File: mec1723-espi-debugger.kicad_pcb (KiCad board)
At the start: 8 copper layers, 62 x 87 mm, 239 parts, among them J1 PinHeader_2x6_P2.54mm_Drill1.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, J10 PinHeader_2x5_P1.27mm_SMD, J11 PinHeader_2x5_P1.27mm_SMD, J12 PinHeader_2x5_P1.27mm_SMD, J13 Tag-Connect_TC2050-IDC-NL_2x5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, J14 Tag-Connect_TC2050-IDC-NL_2x5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, J15 USB-C_GCT_USB4105-GF-A, J2 PinHeader_2x5_P1.27mm_SMD, J3 PinHeader_2x5_P1.27mm_SMD, J4 PinHeader_2x5_P1.27mm_SMD, J5 PinHeader_2x5_P1.27mm_SMD, J6 PinHeader_2x5_P1.27mm_SMD, J7 PinHeader_2x5_P1.27mm_SMD, J8 PinHeader_2x5_P1.27mm_SMD, J9 PinHeader_2x5_P1.27mm_SMD, Q1 DMG1012T-7, SW1 SW_KSC441J70SHLFS_SMD, SW2 SW_KSC441J70SHLFS_SMD, SW3 SW_KSC441J70SHLFS_SMD, U1 MEC1723N-B0-I/SZ, U2 TLV76701_WSON, U3 TPS566231P, U4 MT25QU01GBBB8_SOIC, U5 SN74AC7541_VQFN, U6 SN74AC7541_VQFN, U7 FT2232HL-REEL, Y1 Resonator_32.768kHz_ECX-31B, Y2 Resonator_12MHz_KX-7

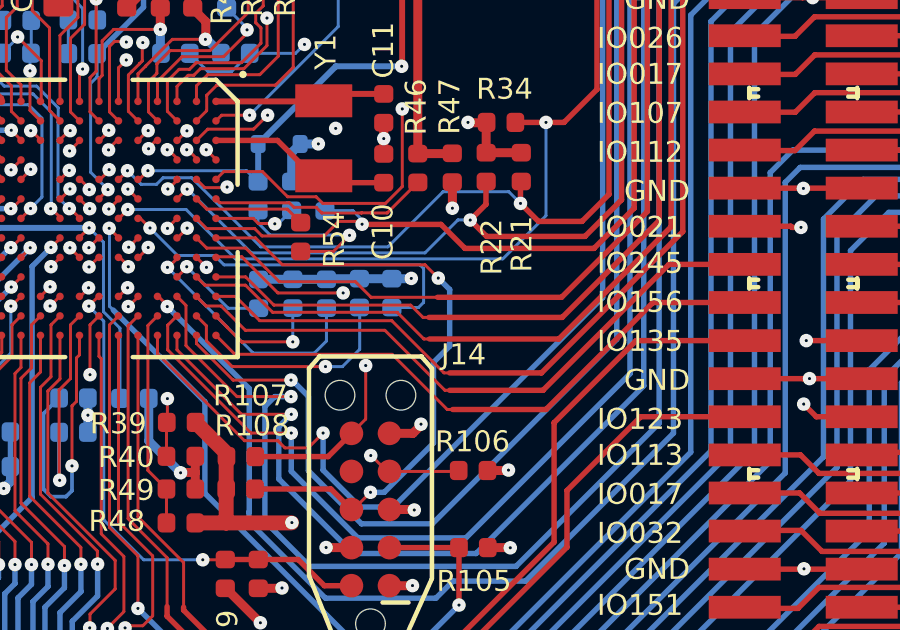
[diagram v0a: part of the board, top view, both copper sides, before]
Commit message: [#103697] pcb: move GPIO156 trace further from the tag-connect hole
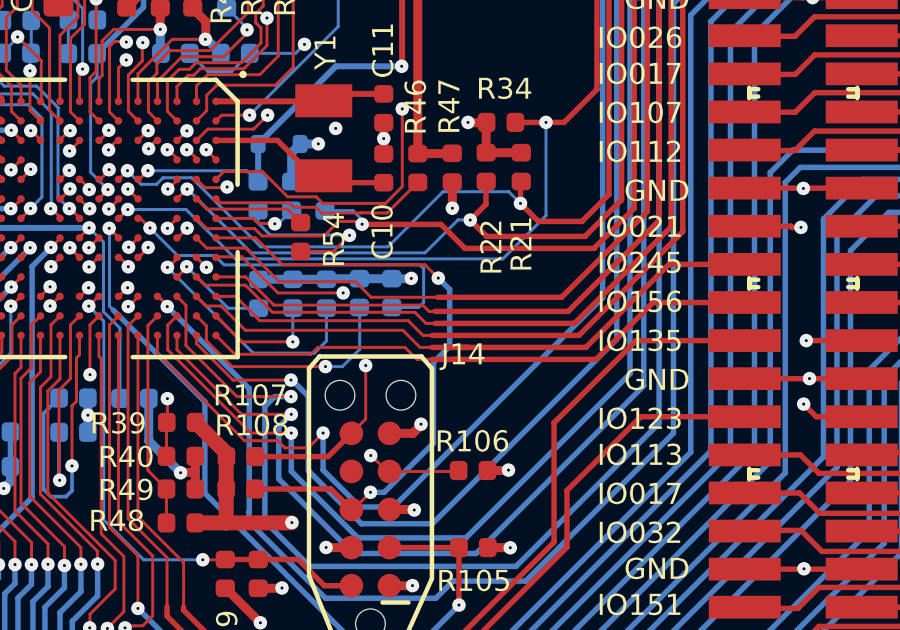
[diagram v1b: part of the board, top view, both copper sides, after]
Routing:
- net /MEC1723/GPIO224: track 44.7 -> 43.6 mm
- net /MEC1723/GPIO156: track 20.1 -> 19.1 mm
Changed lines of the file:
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@@
 	)
 	(segment
-		(start 95.305467 110.656213)
-		(end 98.87168 107.09)
+		(start 98.87168 107.09)
+		(end 101.931 107.09)
+		(width 0.182)
+		(layer "F.Cu")
+		(net "/MEC1723/GPIO156")
+	)
+	(segment
+		(start 92.405467 108.986213)
+		(end 91.505467 108.986213)
 		(width 0.182)
 		(layer "F.Cu")
@@
 	)
 	(segment
-		(start 92.195467 110.656213)
-		(end 92.015467 110.656213)
+		(start 84.305467 108.186213)
+		(end 84.935467 108.816213)
 		(width 0.1)
 		(layer "F.Cu")
@@
 	)
 	(segment
-		(start 92.195467 110.656213)
-		(end 95.305467 110.656213)
+		(start 92.205467 108.986213)
+		(end 92.405467 108.986213)
 		(width 0.182)
 		(layer "F.Cu")
@@
 	)
 	(segment
-		(start 90.175467 108.816213)
-		(end 84.935467 108.816213)
+		(start 90.605467 108.586213)
+		(end 91.005467 108.986213)
 		(width 0.1)
 		(layer "F.Cu")
@@
 	)
 	(segment
-		(start 84.935467 108.816213)
-		(end 84.305467 108.186213)
+		(start 87.475467 108.816213)
+		(end 87.705467 108.586213)
 		(width 0.1)
 		(layer "F.Cu")
@@
 	)
 	(segment
-		(start 98.87168 107.09)
-		(end 101.931 107.09)
+		(start 96.975467 108.986213)
+		(end 98.87168 107.09)
+		(width 0.182)
+		(layer "F.Cu")
+		(net "/MEC1723/GPIO156")
+	)
+	(segment
+		(start 92.405467 108.986213)
+		(end 96.975467 108.986213)
 		(width 0.182)
 		(layer "F.Cu")
@@
 	)
 	(segment
-		(start 92.015467 110.656213)
-		(end 90.175467 108.816213)
+		(start 84.935467 108.816213)
+		(end 87.475467 108.816213)
+		(width 0.1)
+		(layer "F.Cu")
+		(net "/MEC1723/GPIO156")
+	)
+	(segment
+		(start 87.705467 108.586213)
+		(end 90.605467 108.586213)
+		(width 0.1)
+		(layer "F.Cu")
+		(net "/MEC1723/GPIO156")
+	)
+	(segment
+		(start 91.005467 108.986213)
+		(end 91.505467 108.986213)
 		(width 0.1)
 		(layer "F.Cu")
@@
 	)
 	(segment
-		(start 99.772389 76.609291)
-		(end 99.075467 77.306213)
-		(width 0.182)
+		(start 85.295467 106.236213)
+		(end 86.235467 107.176213)
+		(width 0.1)
 		(layer "F.Cu")
 		(net "/MEC1723/GPIO242")
 	)
 	(segment
-		(start 84.305467 106.236213)
-		(end 85.295467 106.236213)
+		(start 91.405467 107.386213)
+		(end 91.605467 107.386213)
 		(width 0.1)
 		(layer "F.Cu")
@@
 	)
 	(segment
-		(start 95.845467 107.586213)
-		(end 91.405467 107.586213)
-		(width 0.182)
+		(start 91.195467 107.176213)
+		(end 91.405467 107.386213)
+		(width 0.1)
 		(layer "F.Cu")
 		(net "/MEC1723/GPIO242")
@@
 	)
 	(segment
-		(start 85.295467 106.236213)
-		(end 86.235467 107.176213)
-		(width 0.1)
-		(layer "F.Cu")
-		(net "/MEC1723/GPIO242")
-	)
-	(segment
-		(start 90.795467 107.176213)
-		(end 91.205467 107.586213)
-		(width 0.1)
-		(layer "F.Cu")
-		(net "/MEC1723/GPIO242")
-	)
-	(segment
 		(start 99.075467 77.306213)
 		(end 99.075467 104.356213)
@@
 	(segment
 		(start 99.075467 104.356213)
-		(end 95.845467 107.586213)
+		(end 96.045467 107.386213)
 		(width 0.182)
 		(layer "F.Cu")
@@
 	(segment
 		(start 86.235467 107.176213)
-		(end 90.795467 107.176213)
+		(end 91.195467 107.176213)
 		(width 0.1)
 		(layer "F.Cu")
@@
 	)
 	(segment
-		(start 91.205467 107.586213)
-		(end 91.405467 107.586213)
-		(width 0.1)
+		(start 96.045467 107.386213)
+		(end 91.605467 107.386213)
+		(width 0.182)
 		(layer "F.Cu")
 		(net "/MEC1723/GPIO242")
 	)
 	(segment
-		(start 99.865467 80.916213)
-		(end 99.865467 104.726213)
+		(start 99.772389 76.609291)
+		(end 99.075467 77.306213)
 		(width 0.182)
 		(layer "F.Cu")
-		(net "/MEC1723/GPIO224")
+		(net "/MEC1723/GPIO242")
 	)
 	(segment
-		(start 84.305467 106.886213)
-		(end 84.955467 106.886213)
+		(start 84.305467 106.236213)
+		(end 85.295467 106.236213)
 		(width 0.1)
 		(layer "F.Cu")
-		(net "/MEC1723/GPIO224")
+		(net "/MEC1723/GPIO242")
 	)
 	(segment
-		(start 85.765467 107.696213)
-		(end 90.165467 107.696213)
+		(start 84.955467 106.886213)
+		(end 85.765467 107.696213)
 		(width 0.1)
 		(layer "F.Cu")
@@
 	)
 	(segment
-		(start 84.955467 106.886213)
-		(end 85.765467 107.696213)
-		(width 0.1)
+		(start 91.505467 108.186213)
+		(end 96.405467 108.186213)
+		(width 0.182)
 		(layer "F.Cu")
 		(net "/MEC1723/GPIO224")
 	)
 	(segment
-		(start 91.905467 109.436213)
-		(end 92.095467 109.436213)
+		(start 91.205467 108.186213)
+		(end 91.505467 108.186213)
 		(width 0.1)
 		(layer "F.Cu")
@@
 	)
 	(segment
-		(start 90.165467 107.696213)
-		(end 91.905467 109.436213)
+		(start 99.865467 80.916213)
+		(end 99.865467 104.726213)
+		(width 0.182)
+		(layer "F.Cu")
+		(net "/MEC1723/GPIO224")
+	)
+	(segment
+		(start 90.715467 107.696213)
+		(end 91.205467 108.186213)
 		(width 0.1)
 		(layer "F.Cu")
@@
 	(segment
 		(start 99.865467 104.726213)
-		(end 95.155467 109.436213)
+		(end 96.405467 108.186213)
 		(width 0.182)
 		(layer "F.Cu")
@@
 	)
 	(segment
-		(start 95.155467 109.436213)
-		(end 92.095467 109.436213)
-		(width 0.182)
+		(start 84.305467 106.886213)
+		(end 84.955467 106.886213)
+		(width 0.1)
 		(layer "F.Cu")
 		(net "/MEC1723/GPIO224")
@@
 	)
 	(segment
+		(start 85.765467 107.696213)
+		(end 90.715467 107.696213)
+		(width 0.1)
+		(layer "F.Cu")
+		(net "/MEC1723/GPIO224")
+	)
+	(segment
 		(start 85.765467 99.496213)
 		(end 86.38 98.88168)
@@
 	)
 	(segment
-		(start 86.192625 107.416213)
+		(start 96.255467 107.786213)
+		(end 91.945467 107.786213)
+		(width 0.182)
+		(layer "F.Cu")
+		(net "/MEC1723/GPIO246")
+	)
+	(segment
+		(start 90.305467 107.416213)
 		(end 90.345467 107.416213)
 		(width 0.1)
@@
 	)
 	(segment
-		(start 99.475467 79.746213)
-		(end 99.475467 104.566213)
+		(start 91.945467 107.786213)
+		(end 91.605467 107.786213)
 		(width 0.182)
 		(layer "F.Cu")
@@
 	)
 	(segment
-		(start 90.345467 107.416213)
-		(end 91.235467 108.306213)
+		(start 86.192625 107.416213)
+		(end 90.305467 107.416213)
 		(width 0.1)
 		(layer "F.Cu")
@@
 	)
 	(segment
-		(start 91.385467 108.306213)
-		(end 91.405467 108.286213)
-		(width 0.1)
+		(start 100.074389 79.147291)
+		(end 99.475467 79.746213)
+		(width 0.182)
 		(layer "F.Cu")
 		(net "/MEC1723/GPIO246")
@@
 	)
 	(segment
-		(start 85.287625 106.511213)
-		(end 86.192625 107.416213)
+		(start 99.475467 79.746213)
+		(end 99.475467 104.566213)
+		(width 0.182)
+		(layer "F.Cu")
+		(net "/MEC1723/GPIO246")
+	)
+	(segment
+		(start 90.935467 107.416213)
+		(end 91.305467 107.786213)
 		(width 0.1)
 		(layer "F.Cu")
@@
 	)
 	(segment
-		(start 101.933314 79.147291)
-		(end 100.074389 79.147291)
+		(start 99.475467 104.566213)
+		(end 96.255467 107.786213)
 		(width 0.182)
 		(layer "F.Cu")
@@
 	)
 	(segment
+		(start 85.287625 106.511213)
+		(end 86.192625 107.416213)
+		(width 0.1)
+		(layer "F.Cu")
+		(net "/MEC1723/GPIO246")
+	)
+	(segment
 		(start 83.930467 106.511213)
 		(end 85.287625 106.511213)
@@
 	)
 	(segment
-		(start 91.235467 108.306213)
-		(end 91.385467 108.306213)
+		(start 91.305467 107.786213)
+		(end 91.945467 107.786213)
 		(width 0.1)
 		(layer "F.Cu")
@@
 	)
 	(segment
-		(start 95.735467 108.306213)
-		(end 91.425467 108.306213)
-		(width 0.182)
+		(start 90.305467 107.416213)
+		(end 90.935467 107.416213)
+		(width 0.1)
 		(layer "F.Cu")
 		(net "/MEC1723/GPIO246")
 	)
 	(segment
-		(start 99.475467 104.566213)
-		(end 95.735467 108.306213)
+		(start 101.933314 79.147291)
+		(end 100.074389 79.147291)
 		(width 0.182)
 		(layer "F.Cu")
@@
 	)
 	(segment
-		(start 100.074389 79.147291)
-		(end 99.475467 79.746213)
+		(start 92.705467 108.586213)
+		(end 96.635467 108.586213)
 		(width 0.182)
 		(layer "F.Cu")
-		(net "/MEC1723/GPIO246")
+		(net "/MEC1723/GPIO245")
+	)
+	(segment
+		(start 99.40268 105.819)
+		(end 101.932 105.819)
+		(width 0.182)
+		(layer "F.Cu")
+		(net "/MEC1723/GPIO245")
 	)
 	(segment
-		(start 91.935467 110.016213)
-		(end 92.095467 110.016213)
+		(start 83.655467 106.886213)
+		(end 83.975467 107.206213)
 		(width 0.1)
 		(layer "F.Cu")
@@
 	)
 	(segment
-		(start 95.205467 110.016213)
-		(end 99.40268 105.819)
+		(start 92.705467 108.586213)
+		(end 91.505467 108.586213)
 		(width 0.182)
 		(layer "F.Cu")
@@
 	)
 	(segment
-		(start 92.095467 110.016213)
-		(end 95.205467 110.016213)
+		(start 91.905467 108.586213)
+		(end 92.705467 108.586213)
 		(width 0.182)
 		(layer "F.Cu")
@@
 	)
 	(segment
-		(start 89.935467 108.016213)
-		(end 91.935467 110.016213)
+		(start 83.975467 107.206213)
+		(end 84.475467 107.206213)
 		(width 0.1)
 		(layer "F.Cu")
@@
 	)
 	(segment
-		(start 84.475467 107.206213)
-		(end 85.285467 108.016213)
-		(width 0.1)
+		(start 96.635467 108.586213)
+		(end 99.40268 105.819)
+		(width 0.182)
 		(layer "F.Cu")
 		(net "/MEC1723/GPIO245")
 	)
 	(segment
-		(start 85.285467 108.016213)
-		(end 89.935467 108.016213)
+		(start 91.105467 108.586213)
+		(end 91.505467 108.586213)
 		(width 0.1)
 		(layer "F.Cu")
@@
 	)
 	(segment
-		(start 83.655467 106.886213)
-		(end 83.975467 107.206213)
+		(start 90.535467 108.016213)
+		(end 91.105467 108.586213)
 		(width 0.1)
 		(layer "F.Cu")
@@
 	)
 	(segment
-		(start 99.40268 105.819)
-		(end 101.932 105.819)
-		(width 0.182)
+		(start 85.285467 108.016213)
+		(end 90.535467 108.016213)
+		(width 0.1)
 		(layer "F.Cu")
 		(net "/MEC1723/GPIO245")
 	)
 	(segment
-		(start 83.975467 107.206213)
-		(end 84.475467 107.206213)
+		(start 84.475467 107.206213)
+		(end 85.285467 108.016213)
 		(width 0.1)
 		(layer "F.Cu")
